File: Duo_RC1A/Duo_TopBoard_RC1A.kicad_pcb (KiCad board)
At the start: 2 copper layers, 169.2 x 131.9 mm, 106 parts, among them CN1 CONN_PANNEL_2X2, CN2 CONN_PANNEL_2X2, P1 HEADER_180_2.54_10X2, P2 KK3.96_2, P3 HEADER_180_2.54_4X1, P4 HEADER_180_2.54_5X2, Q1 MMBT3904, Q2 MMBT3904, SW1 SW_PUSH, U1 LPC1754FBD80, U2 TLV803, U3 74LVC1G125, U4 NCP1117DT33G, X1 10MHz

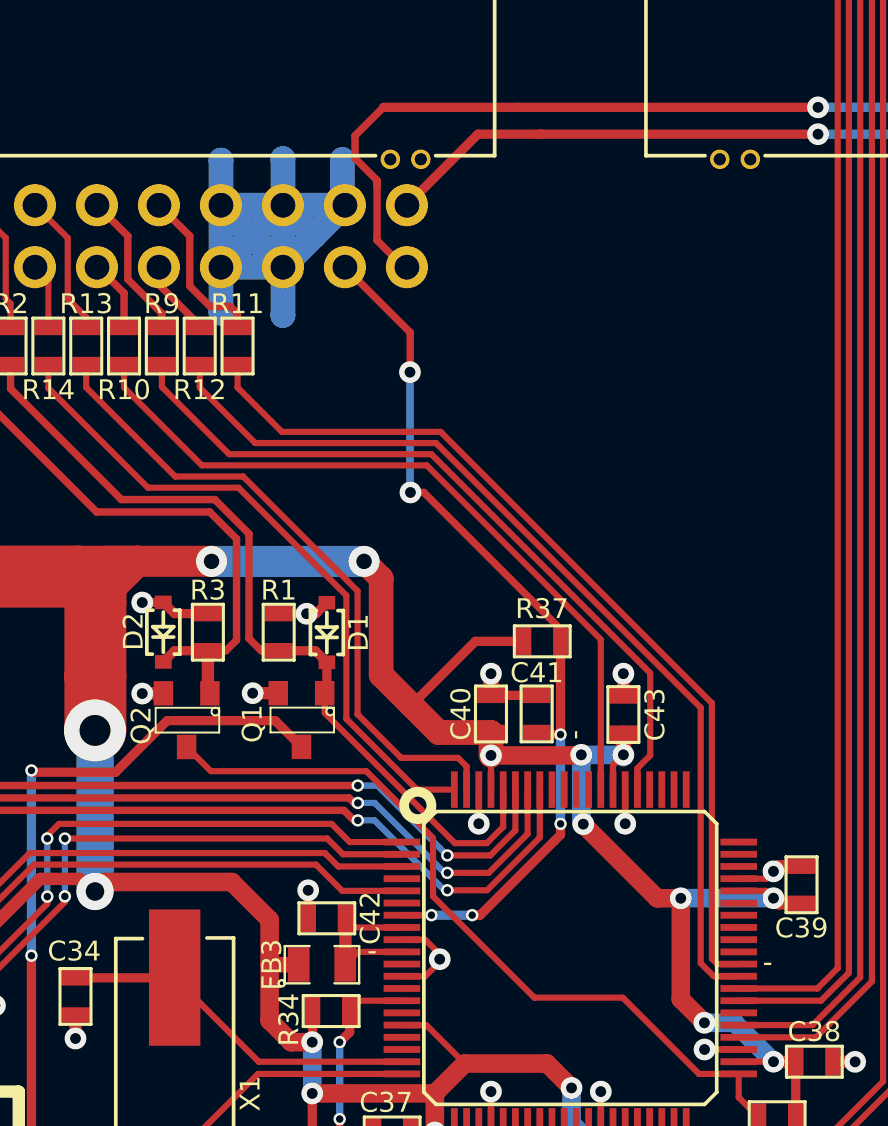
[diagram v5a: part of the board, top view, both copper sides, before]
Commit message: wip issue #13: updated TopBoard pcb traces (removal of UI UART)
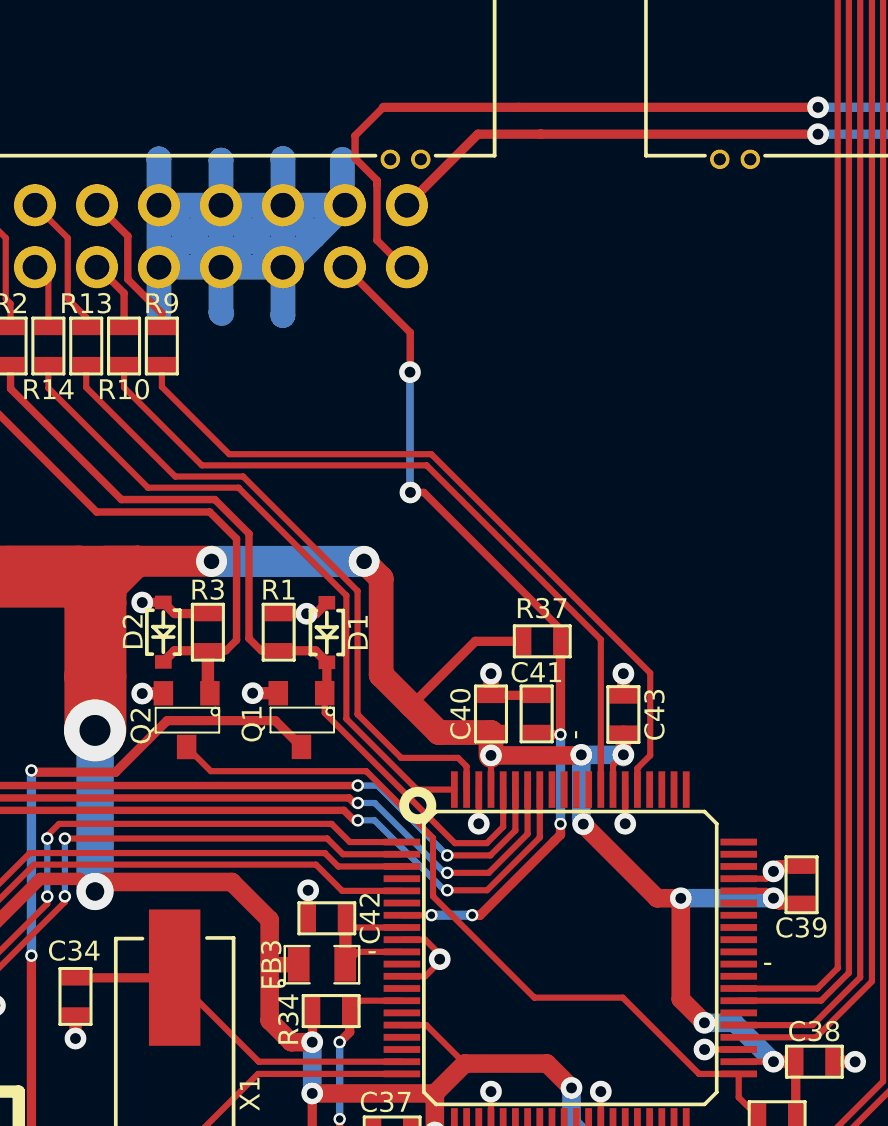
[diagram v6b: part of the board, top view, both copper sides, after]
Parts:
- removed R11, R12: 100R, Duo_Audio_HMI_RC1A:SM0603
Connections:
- P1 pad 11: Net-(P1-Pad11) -> DGND
- P1 pad 12: Net-(P1-Pad12) -> DGND
- U1 pad 49: RXD2_UC_UI -> Net-(U1-Pad49)
- U1 pad 50: TXD2_UC_UI -> Net-(U1-Pad50)
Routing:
- net RXD2_UC_UI: track 39.1 -> 0.00 mm
- net TXD2_UC_UI: track 37.4 -> 0.00 mm
- net DGND: track 685.9 -> 705.2 mm
- net Net-(P1-Pad11): track 7.19 -> 0.00 mm
- net Net-(P1-Pad12): track 3.16 -> 0.00 mm

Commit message: fix issue #4: renaming signals.
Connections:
- net DTR_HOST_FIRMWARE renamed DTR_HMI
- net RTS_HOST_FIRMWARE renamed RTS_HMI
- net RXD0_UC_FIRMWARE renamed RXD0_HMI
- net RXD3_UC_CONSOLE renamed RXD3_CONSOLE
- net TXD0_UC_FIRMWARE renamed TXD0_HMI
- net TXD3_UC_CONSOLE renamed TXD3_CONSOLE

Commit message: fix issue #8: (Rename serial interface signal names)
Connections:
- net DTR_HMI renamed UC_RESET_CONTROL
- net RTS_HMI renamed UC_ISP_MODE_ENABLE
- net RXD0_HMI renamed RXD0_UI
- net TXD0_HMI renamed TXD0_UI
